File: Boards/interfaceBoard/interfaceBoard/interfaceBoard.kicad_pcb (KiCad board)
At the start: 2 copper layers, 100 x 100 mm, 34 parts, among them J1 12V input (molex), J2 Barrel_Jack_Switch, J3 Interface With Arduino, J4 Conn_02x17_Odd_Even, J5 DaisyCainOut, J6 Conn_02x17_Odd_Even, SW1 SW_SPDT, U1 74HC595, U10 74HC595, U11 TBD62783A, U12 74HC165, U2 TBD62783A, U3 74HC165, U4 74HC595, U5 TBD62783A, U6 74HC165, U7 74HC595, U8 TBD62783A, U9 74HC165

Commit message: DRC PASSED
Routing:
- net CLK: track 119.6 -> 579.9 mm
- net 5V+: track 180.2 -> 479.6 mm
- net LOAD: track 0.00 -> 201.6 mm
- net /MOSI_sheet3/QH': track 0.00 -> 165.2 mm, vias 0 -> 2
- net /MISO: track 0.00 -> 106.6 mm
- net /STATUS: track 41.5 -> 141.1 mm
- net LATCH: track 134.6 -> 232.2 mm
- net /MISO_sheet3/SerIn: track 0.00 -> 84.4 mm, vias 0 -> 2
- net GND: track 243.9 -> 305.9 mm, vias 6 -> 41
- net /MISO_sheet1/SerIn: track 0.00 -> 50.9 mm
- net /MISO_sheet2/SerIn: track 0.00 -> 43.6 mm, vias 0 -> 2
- net /MISO_sheet/SerIn: track 0.00 -> 36.1 mm, vias 0 -> 1
- net Net-(D3-A): track 0.00 -> 4.14 mm
- net Net-(RN1-R4.1): track 25.4 -> 28.5 mm
- net Net-(RN1-R3.1): track 21.1 -> 24.1 mm
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- added copper zone on B.Cu, net GND
- added copper zone on F.Cu, net GND

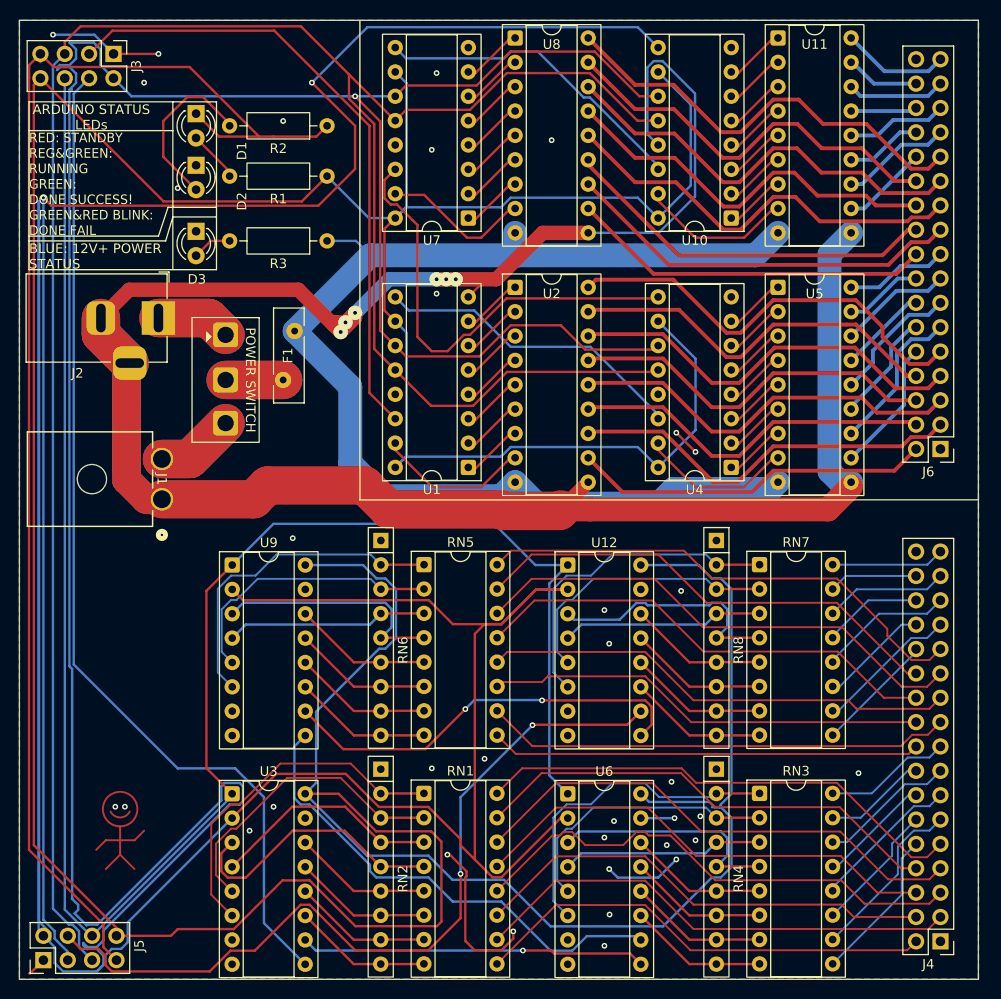
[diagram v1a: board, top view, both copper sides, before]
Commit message: FINALISH
need to respec the fuse and switch (or just accept lower current)
forgot to put in decoupling capacitors for shift registers
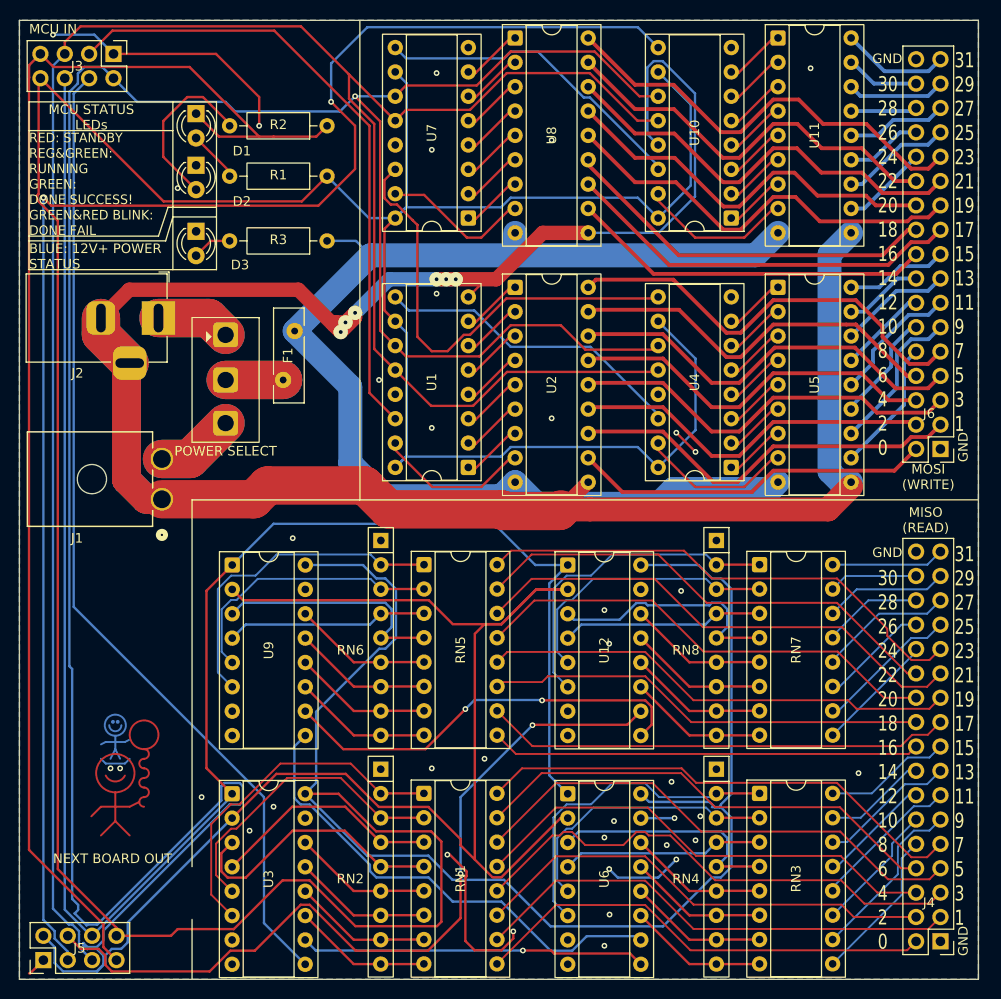
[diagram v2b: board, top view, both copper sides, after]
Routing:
- net CLK: track 579.9 -> 417.8 mm
- net GND: track 305.9 -> 321.3 mm, vias 41 -> 42
- net /MISO: track 106.6 -> 103.1 mm
- net /MOSI_sheet3/QH': track 165.2 -> 163.6 mm
- net /STATUS: track 141.1 -> 140.3 mm
- net (no net): vias 0 -> 2
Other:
- board text added: "30 28 26 24 22 20 18 16 14 12 10 8 6 4 2 0"
- board text added: "31 29 27 25 23 21 19 17 15 13 11 9 7 5 3 1"
- board text added: "GND"
- board text added: "MCU IN"
- board text added: "MCU STATUS LEDs"
- board text added: "MISO (READ)"
- board text added: "MOSI (WRITE)"
- board text added: "NEXT BOARD OUT"
- board text removed: "ARDUINO STATUS LEDs"

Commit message: INTERFACE manufacture
V1 ready for interface
Everything TH.
after this commit I will experiment with hybrid THT SMD setup
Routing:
- net GND: track 321.3 -> 325.2 mm, vias 42 -> 46
